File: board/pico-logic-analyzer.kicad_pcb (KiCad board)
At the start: 4 copper layers, 85 x 57.5 mm, 62 parts, among them J1 Conn_02x03_Odd_Even, J10 Conn_02x03_Odd_Even, J11 Conn_01x01, J2 Conn_02x03_Odd_Even, J3 Conn_02x03_Odd_Even, J4 Conn_02x03_Odd_Even, J5 Conn_02x03_Odd_Even, J6 Conn_02x03_Odd_Even, J7 Conn_02x03_Odd_Even, J8 Conn_02x03_Odd_Even, J9 Conn_02x03_Odd_Even, SW1 SW_Push, SW2 SW_DIP_x04, SW3 SW_DIP_x04, SW4 SW_DIP_x04, U1 LM2665M6, U2 LM4040DBZ-5, U3 TXB0104PW (fit with U104), U4 TXB0104PW (fit with U104), U5 TXB0104PW (fit with U104)

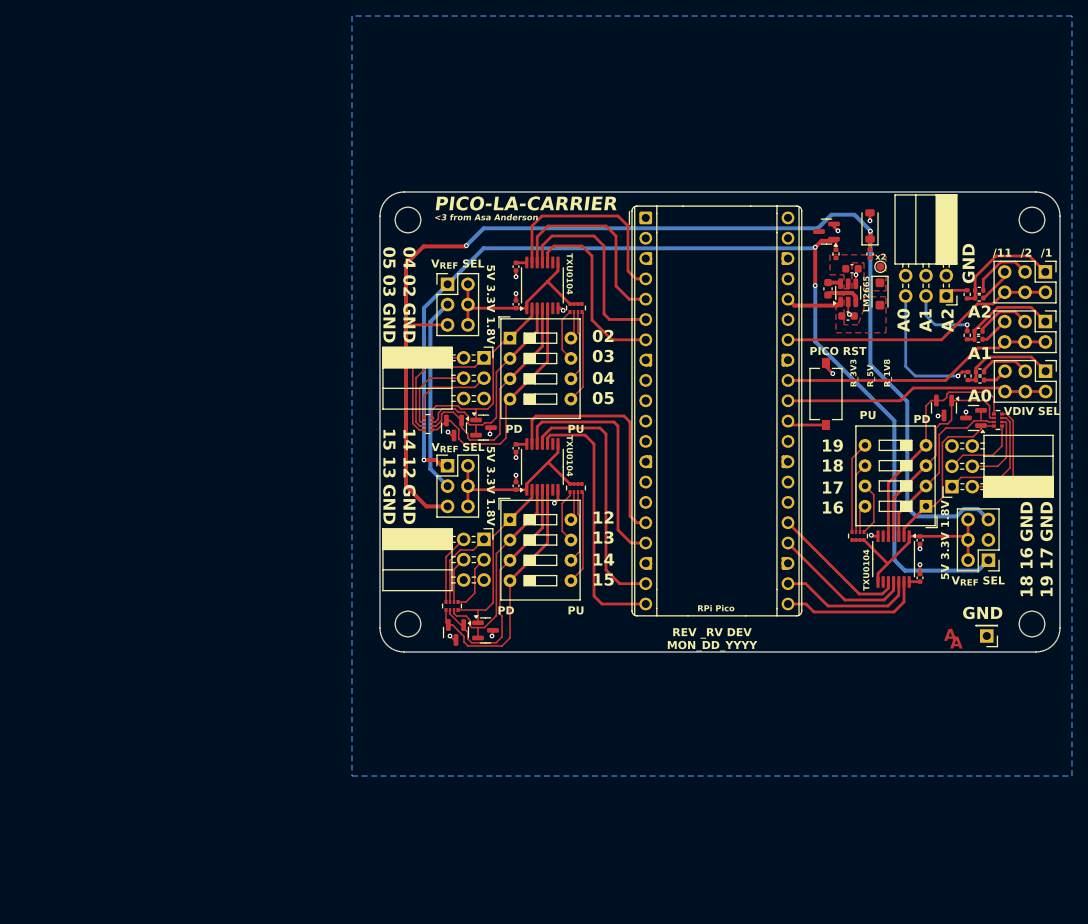
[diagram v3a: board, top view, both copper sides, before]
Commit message: layout overhaul backside pico now, which significantly reduces the size of the board and lets me do less suspect routing need to finish power delivery network for 3.3v, 5v reference, and 1.8v reference rails
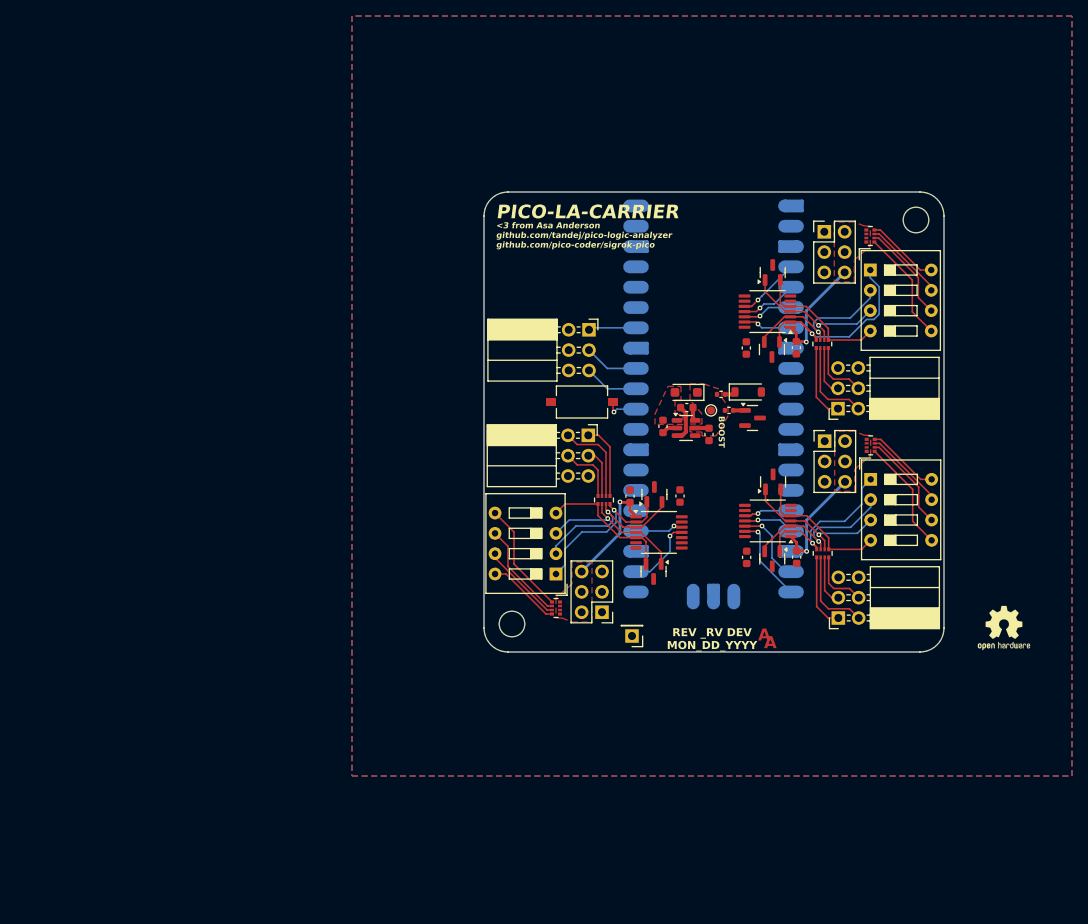
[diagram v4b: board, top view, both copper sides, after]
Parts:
- removed A1: RaspberryPi_Pico, Module_RaspberryPi_Pico:RaspberryPi_Pico_Common_THT
- removed H2, H3: MountingHole, MountingHole:MountingHole_3.2mm_M3
- removed H5: MountingHole, Symbol:OSHW-Logo2_7.3x6mm_SilkScreen
- removed H6: MountingHole, Symbol:KiCad-Logo2_5mm_SilkScreen
- removed J10, J8, J9: Conn_02x03_Odd_Even, Connector_PinHeader_2.54mm:PinHeader_2x03_P2.54mm_Vertical
- removed R16, R17, R19, R20, R22, R23: 100 1%, Resistor_SMD:R_0402_1005Metric
- removed R18, R21, R24: 1k 1%, Resistor_SMD:R_0402_1005Metric
- added A2: RaspberryPi_Pico, asa-lib:RaspberryPi_Pico_SMD, B.Cu at (167.7, 77.9)
- added G1: oshw!, Symbol:OSHW-Logo2_7.3x6mm_SilkScreen, F.Cu at (204.0, 106.5)
- C4, C5, C6, C7, C8, C9: value 1 uF -> 4.7 uF; footprint Capacitor_SMD:C_0402_1005Metric -> Capacitor_SMD:C_0603_1608Metric
- moved RN5 50.3 mm to (181.3, 71.0), turned to -90 degrees
- moved RN6 50.3 mm to (154.0, 90.5), turned to 90 degrees
- moved J6 48.7 mm to (153.8, 104.5)
- moved J4 47.5 mm to (181.5, 57.0)
- moved J2 47.2 mm to (181.6, 83.1)
- moved SW4 47.0 mm to (148.0, 99.8)
- moved RN4 46.8 mm to (181.3, 97.2), turned to -90 degrees
- moved J7 45.9 mm to (152.0, 82.4), turned to 0 degrees
- moved SW3 45.8 mm to (187.3, 61.8)
- moved J3 45.4 mm to (183.3, 105.2), turned to 180 degrees
- moved SW2 45.4 mm to (187.3, 87.9)
- moved J1 44.9 mm to (152.1, 69.2), turned to 0 degrees
- moved J5 44.7 mm to (183.2, 79.1), turned to 180 degrees
- moved J11 44.3 mm to (157.5, 107.5)
- moved D5 44.3 mm to (175.1, 62.1), turned to 90 degrees
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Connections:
- J1 pad 1: /A2_IN -> /A2
- J1 pad 3: /A1_IN -> /A1
- J1 pad 5: /A0_IN -> /A0
- J2 pad 1: /+5V_REG -> +3V3
- J2 pad 3: +3V3 -> /+1.8V_REG
- J2 pad 5: /+1.8V_REG -> /+5V_REG
- J3 pad 1: /Buffer Block A/A2 -> /Buffer Block A/A0
- J3 pad 2: /Buffer Block A/A3 -> /Buffer Block A/A1
- J3 pad 3: /Buffer Block A/A0 -> /Buffer Block A/A2
- J3 pad 4: /Buffer Block A/A1 -> /Buffer Block A/A3
- J4 pad 1: /+5V_REG -> +3V3
- J4 pad 3: +3V3 -> /+1.8V_REG
- J4 pad 5: /+1.8V_REG -> /+5V_REG
- J5 pad 1: /Buffer Block B/A2 -> /Buffer Block B/A0
- J5 pad 2: /Buffer Block B/A3 -> /Buffer Block B/A1
- J5 pad 3: /Buffer Block B/A0 -> /Buffer Block B/A2
- J5 pad 4: /Buffer Block B/A1 -> /Buffer Block B/A3
- J6 pad 1: /+5V_REG -> +3V3
- J6 pad 3: +3V3 -> /+1.8V_REG
- J6 pad 5: /+1.8V_REG -> /+5V_REG
- J7 pad 1: /Buffer Block C/A2 -> /Buffer Block C/A0
- J7 pad 2: /Buffer Block C/A3 -> /Buffer Block C/A1
- J7 pad 3: /Buffer Block C/A0 -> /Buffer Block C/A2
- J7 pad 4: /Buffer Block C/A1 -> /Buffer Block C/A3
- SW2 pad 5: Net-(RN1D-R4.1) -> Net-(RN1A-R1.1)
- SW2 pad 6: Net-(RN1C-R3.1) -> Net-(RN1B-R2.1)
- SW2 pad 7: Net-(RN1A-R1.1) -> Net-(RN1C-R3.1)
- SW2 pad 8: Net-(RN1B-R2.1) -> Net-(RN1D-R4.1)
- SW3 pad 5: Net-(RN2D-R4.1) -> Net-(RN2A-R1.1)
- SW3 pad 6: Net-(RN2C-R3.1) -> Net-(RN2B-R2.1)
- SW3 pad 7: Net-(RN2A-R1.1) -> Net-(RN2C-R3.1)
- SW3 pad 8: Net-(RN2B-R2.1) -> Net-(RN2D-R4.1)
- SW4 pad 5: Net-(RN3D-R4.1) -> Net-(RN3A-R1.1)
- SW4 pad 6: Net-(RN3C-R3.1) -> Net-(RN3B-R2.1)
- SW4 pad 7: Net-(RN3A-R1.1) -> Net-(RN3C-R3.1)
- SW4 pad 8: Net-(RN3B-R2.1) -> Net-(RN3D-R4.1)
- U3 pad 10: /A3 / IO15 -> /IO12
- U3 pad 11: /A2 / IO14 -> /IO13
- U3 pad 12: /A1 / IO13 -> /IO14
- U3 pad 13: /A0 / IO12 -> /IO15
- U3 pad 8: /Buffer Block A/VCCA_SEL -> +3V3
- U4 pad 10: /B3 / IO05 -> /IO02
- U4 pad 11: /B2 / IO04 -> /IO03
- U4 pad 12: /B1 / IO03 -> /IO04
- U4 pad 13: /B0 / IO02 -> /IO05
- U4 pad 8: /Buffer Block B/VCCA_SEL -> +3V3
- U5 pad 10: /C3 / IO019 -> /IO16
- U5 pad 11: /C2 / IO018 -> /IO17
- U5 pad 12: /C1 / IO17 -> /IO18
- U5 pad 13: /C0 / IO16 -> /IO19
- U5 pad 8: /Buffer Block C/VCCA_SEL -> +3V3
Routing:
- net /+1.8V_REG: track 151.0 -> 1.35 mm, vias 2 -> 0
- net /+5V_REG: track 134.6 -> 1.49 mm, vias 3 -> 0
- net +3V3: track 35.7 -> 0.00 mm
- net /A2_DIV: track 34.6 -> 0.00 mm
- net /A1_DIV: track 34.2 -> 0.00 mm
- net /A3 / IO15: track 33.1 -> 0.00 mm
- net /A0_DIV: track 32.4 -> 0.00 mm
- net /A2 / IO14: track 32.3 -> 0.00 mm
- net /A1 / IO13: track 29.9 -> 0.00 mm
- net /A0 / IO12: track 29.8 -> 0.00 mm
- net /B0 / IO02: track 25.8 -> 0.00 mm
- net /B2 / IO04: track 24.8 -> 0.00 mm
- net /B1 / IO03: track 24.8 -> 0.00 mm
- net /B3 / IO05: track 23.4 -> 0.00 mm
- net GND: track 21.0 -> 1.99 mm, vias 20 -> 0
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- added copper zone on F.Cu, net /Buffer Block A/VCCA_SEL
- added copper zone on F.Cu, net /Buffer Block B/VCCA_SEL
- added copper zone on F.Cu, net /Buffer Block C/VCCA_SEL
- added copper zone on F.Cu, net GND
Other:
- board size 85 x 57.5 mm -> 57.5 x 57.5 mm
- board text added: "<3 from Asa Anderson github.com/tandej/pico-logic-analyzer github.com/pico-coder/sigrok-pico"
- board text added: "BOOST"
- board text removed: "/1"
- board text removed: "/11"
- board text removed: "/2"
- board text removed: "02"
- board text removed: "03"
- board text removed: "04"
- board text removed: "05"
- board text removed: "1.8V"
- board text removed: "12"
- board text removed: "13"
- board text removed: "14"
- board text removed: "15"
- board text removed: "16"
- board text removed: "17"
- board text removed: "18"
- board text removed: "19"
- board text removed: "3.2mm Ø"
- board text removed: "3.3V"
- board text removed: "3.5mm"
- board text removed: "50.5mm"
- board text removed: "5V"
- board text removed: "78mm"
- board text removed: ":3"
- board text removed: "<3 from Asa Anderson"
- board text removed: "A0"
- board text removed: "A1"
- board text removed: "A2"
- board text removed: "GND"
- board text removed: "LM2665"
- board text removed: "PD"
- board text removed: "PICO RST"
- board text removed: "PU"
- board text removed: "RPi Pico"
- board text removed: "R_1V8"
- board text removed: "R_3V3"
- board text removed: "R_5V"
- board text removed: "TXU0104"
- board text removed: "VDIV SEL"
- board text removed: "V_{REF} SEL"
- board text removed: "github.com/tandej/pico-logic-analyzer github.com/pico-coder/sigrok-pico github.com/recursivenomad/ki-lime-pi-to-go"
- board text removed: "x2"

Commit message: finish power routing also 9.0 import! jobsets coming soon
export is very broken at this point, do not trust the artifacts
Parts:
- moved J11 21.5 mm to (179.0, 107.2)
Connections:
- J2 pad 1: +3V3 -> /+1.8V_REG
- J2 pad 3: /+1.8V_REG -> /+5V_REG
- J2 pad 5: /+5V_REG -> +3V3
- J4 pad 1: +3V3 -> /+1.8V_REG
- J4 pad 3: /+1.8V_REG -> /+5V_REG
- J4 pad 5: /+5V_REG -> +3V3
- J6 pad 1: +3V3 -> /+1.8V_REG
- J6 pad 3: /+1.8V_REG -> /+5V_REG
- J6 pad 5: /+5V_REG -> +3V3
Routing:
- net +3V3: track 0.00 -> 123.4 mm, vias 0 -> 3
- net /+1.8V_REG: track 1.35 -> 93.5 mm, vias 0 -> 5
- net /+5V_REG: track 1.49 -> 83.4 mm, vias 0 -> 2
- net /IO16: track 0.00 -> 9.71 mm, vias 0 -> 1
- net /IO19: track 0.00 -> 6.17 mm, vias 0 -> 1
- net GND: track 1.99 -> 4.66 mm, vias 0 -> 87
- removed copper zone on F.Cu, net +3V3
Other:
- copper layers 4 -> 13
- board text removed: "A"

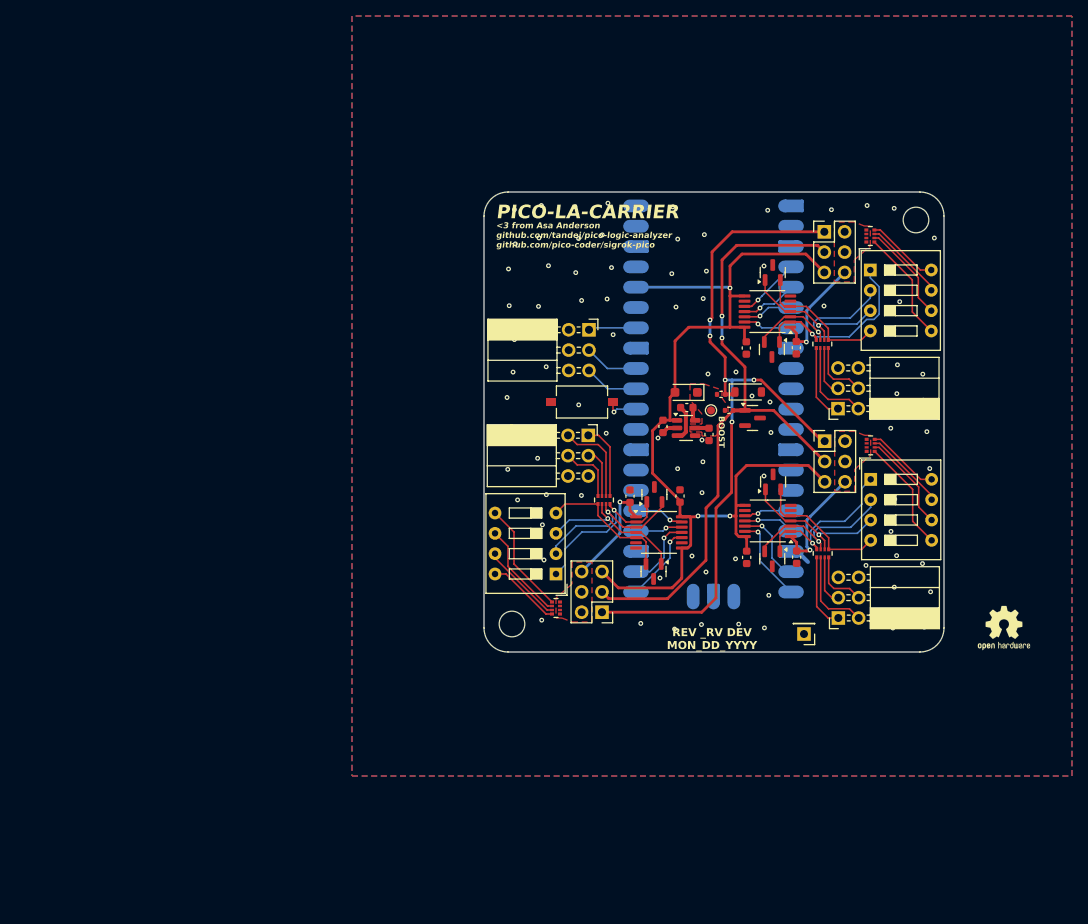
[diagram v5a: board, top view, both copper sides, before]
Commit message: backup commit before project structure overhaul
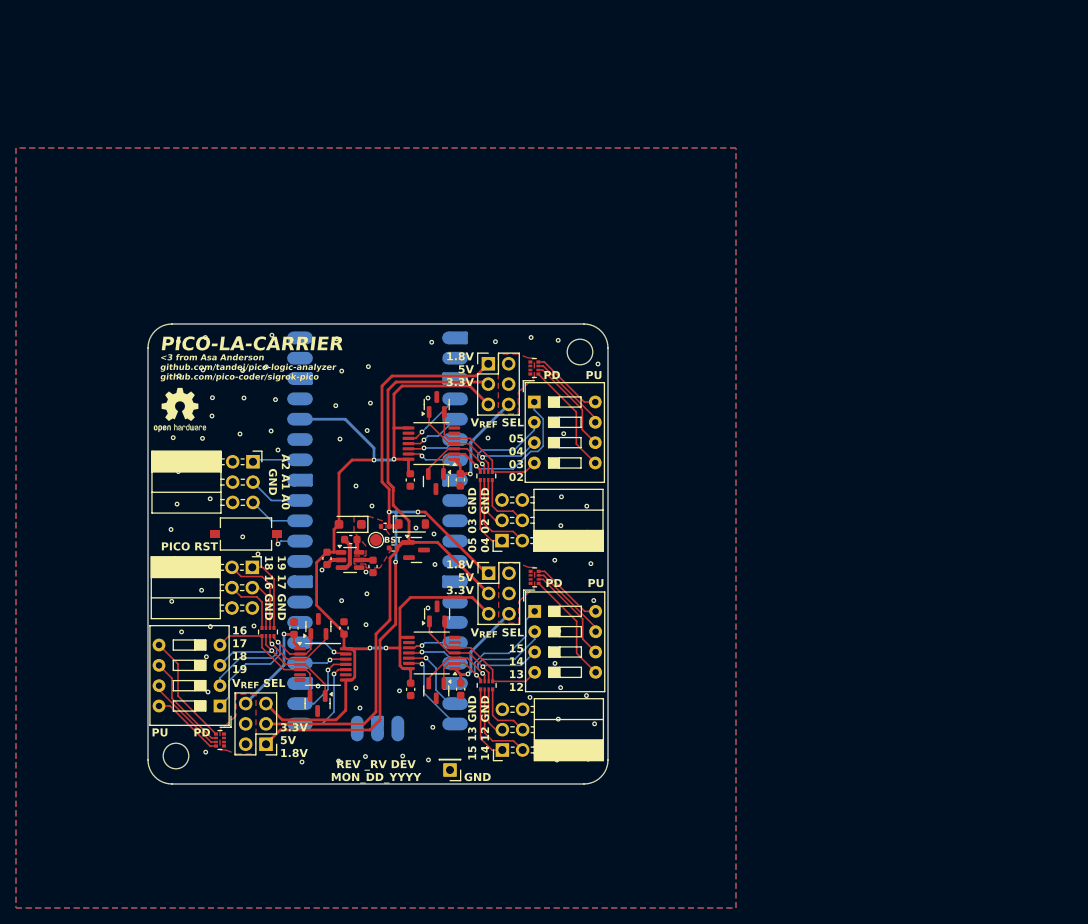
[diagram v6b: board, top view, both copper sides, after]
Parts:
- TP1: renamed from TP4; footprint TestPoint:TestPoint_Pad_D1.0mm -> TestPoint:TestPoint_Pad_D1.5mm
- moved G1 106.5 mm to (101.0, 79.2)
- moved J8 47.4 mm to (134.8, 124.2)
- moved R2 45.4 mm to (127.6, 96.5)
- moved D6 45.1 mm to (118.3, 106.3)
- moved U5 45.1 mm to (118.9, 111.0)
- moved A1 45.1 mm to (125.7, 94.4)
- moved C1 45.1 mm to (129.8, 88.0)
- moved C2 45.1 mm to (136.0, 88.0)
- moved C3 45.1 mm to (122.3, 95.5)
- moved C4 45.1 mm to (119.4, 97.8)
- moved C5 45.1 mm to (125.1, 98.8)
- moved C6 45.1 mm to (115.2, 106.5)
- moved C7 45.1 mm to (121.5, 106.5)
- moved C8 45.1 mm to (129.8, 114.2)
- moved C9 45.1 mm to (136.1, 114.1)
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- renumbered A2 to A1, C7 to C1, C6 to C2, C2 to C3, C1 to C4, C3 to C5, C8 to C6, C9 to C7, C5 to C8, C4 to C9, D5 to D1, D8 to D2, D2 to D3, D1 to D4, D4 to D5, D9 to D6, D6 to D8, H4 to H2, J4 to J1, J1 to J2, J5 to J3, J7 to J4, J2 to J5, J3 to J7, J11 to J8, R3 to R2, RN2 to RN1, RN5 to RN2, RN1 to RN3, RN6 to RN4, RN4 to RN5, RN3 to RN6, SW3 to SW1, SW1 to SW2, SW2 to SW3, U4 to U1, U1 to U3, U3 to U4
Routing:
- net /+1.8V_REG: track 93.5 -> 91.3 mm, vias 5 -> 3
- net GND: track 4.66 -> 2.78 mm
- net /Buffer Block A/VCCA_SEL: track 14.5 -> 12.7 mm
- net /IO16: track 9.71 -> 11.3 mm
- net +3V3: track 123.4 -> 124.0 mm, vias 3 -> 4
- net /+5V_REG: track 83.4 -> 83.6 mm, vias 2 -> 0
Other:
- copper layers 13 -> 4
- board text added: "05 03 GND 04 02 GND"
- board text added: "05 04 03 02"
- board text added: "1.8V 5V 3.3V"
- board text added: "15 13 GND 14 12 GND"
- board text added: "15 14 13 12"
- board text added: "16 17 18 19"
- board text added: "19 17 GND 18 16 GND"
- board text added: "3.3V 5V 1.8V"
- board text added: "A2 A1 A0 GND"
- board text added: "BST"
- board text added: "GND"
- board text added: "PD"
- board text added: "PICO RST"
- board text added: "PU"
- board text added: "V_{REF} SEL"
- board text removed: "BOOST"
